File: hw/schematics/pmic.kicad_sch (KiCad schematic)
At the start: 40 parts, among them J1 TYPE-C-31-M-13C, J2 Conn_01x02, U2 NPM1300-QEAA-R

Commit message: apply 0603 footprint
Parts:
- C1, C10, C2, C3, C4, C5, C6, C7, C8, C9, R1, R13, R14, R2, R4, rC1, rC10, rC2, rC3, rC4, rC5, rC6, rC7, rC8, rC9, rR1, rR13, rR14, rR2, rR4: footprint (none) -> Alidade:SMD_0603
- L1, L2, rL1, rL2: value 2.2u -> 2.2uH; footprint (none) -> Alidade:SMD_0603
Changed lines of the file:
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@@
 			)
 		)
-		(property "Value" "2.2u"
+		(property "Value" "2.2uH"
 			(at 44.4181 145.034 90)
 			(effects
@@
 			)
 		)
-		(property "Footprint" ""
+		(property "Footprint" "Alidade:SMD_0603"
 			(at 44.45 143.51 0)
 			(effects
@@
 			)
 		)
-		(property "Footprint" ""
+		(property "Footprint" "Alidade:SMD_0603"
 			(at 367.03 148.59 0)
 			(effects
@@
 			)
 		)
-		(property "Footprint" ""
+		(property "Footprint" "Alidade:SMD_0603"
 			(at 265.43 148.59 0)
 			(effects
@@
 			)
 		)
-		(property "Footprint" ""
+		(property "Footprint" "Alidade:SMD_0603"
 			(at 374.65 148.59 0)
 			(effects
@@
 			)
 		)
-		(property "Footprint" ""
+		(property "Footprint" "Alidade:SMD_0603"
 			(at 212.09 236.22 0)
 			(effects
@@
 			)
 		)
-		(property "Value" "2.2u"
+		(property "Value" "2.2uH"
 			(at 139.446 148.59 90)
 			(effects
@@
 			)
 		)
-		(property "Footprint" ""
+		(property "Footprint" "Alidade:SMD_0603"
 			(at 139.7 147.32 0)
 			(effects
@@
 			)
 		)
-		(property "Footprint" ""
+		(property "Footprint" "Alidade:SMD_0603"
 			(at 273.05 148.59 0)
 			(effects
@@
 			)
 		)
-		(property "Footprint" ""
+		(property "Footprint" "Alidade:SMD_0603"
 			(at 355.6 49.53 0)
 			(effects
@@
 			)
 		)
-		(property "Footprint" ""
+		(property "Footprint" "Alidade:SMD_0603"
 			(at 257.81 148.59 0)
 			(effects
@@
 			)
 		)
-		(property "Footprint" ""
+		(property "Footprint" "Alidade:SMD_0603"
 			(at 351.79 148.59 0)
 			(effects
@@
 			)
 		)
-		(property "Footprint" ""
+		(property "Footprint" "Alidade:SMD_0603"
 			(at 250.19 148.59 0)
 			(effects
@@
 			)
 		)
-		(property "Footprint" ""
+		(property "Footprint" "Alidade:SMD_0603"
 			(at 359.41 148.59 0)
 			(effects
@@
 			)
 		)
-		(property "Footprint" ""
+		(property "Footprint" "Alidade:SMD_0603"
 			(at 284.48 48.26 0)
 			(effects
@@
 			)
 		)
-		(property "Footprint" ""
+		(property "Footprint" "Alidade:SMD_0603"
 			(at 205.74 236.22 0)
 			(effects
@@
 			)
 		)
-		(property "Footprint" ""
+		(property "Footprint" "Alidade:SMD_0603"
 			(at 142.24 153.67 0)
 			(effects
@@
 			)
 		)
-		(property "Footprint" ""
+		(property "Footprint" "Alidade:SMD_0603"
 			(at 295.91 148.59 0)
 			(effects
@@
 			)
 		)
-		(property "Footprint" ""
+		(property "Footprint" "Alidade:SMD_0603"
 			(at 321.31 148.59 0)
 			(effects
@@
 			)
 		)
-		(property "Footprint" ""
+		(property "Footprint" "Alidade:SMD_0603"
 			(at 46.99 149.86 0)
 			(effects
@@
 			)
 		)
-		(property "Footprint" ""
+		(property "Footprint" "Alidade:SMD_0603"
 			(at 288.29 148.59 0)
 			(effects
@@
 			)
 		)
-		(property "Footprint" ""
+		(property "Footprint" "Alidade:SMD_0603"
 			(at 87.63 148.59 0)
 			(effects
@@
 			)
 		)
-		(property "Footprint" ""
+		(property "Footprint" "Alidade:SMD_0603"
 			(at 328.93 148.59 0)
 			(effects
@@
 			)
 		)
-		(property "Footprint" ""
+		(property "Footprint" "Alidade:SMD_0603"
 			(at 234.95 148.59 0)
 			(effects
@@
 			)
 		)
-		(property "Footprint" ""
+		(property "Footprint" "Alidade:SMD_0603"
 			(at 279.4 237.49 0)
 			(effects
@@
 			)
 		)
-		(property "Value" "2.2u"
+		(property "Value" "2.2uH"
 			(at 84.582 144.018 90)
 			(effects
@@
 			)
 		)
-		(property "Footprint" ""
+		(property "Footprint" "Alidade:SMD_0603"
 			(at 85.09 142.24 0)
 			(effects
@@
 			)
 		)
-		(property "Footprint" ""
+		(property "Footprint" "Alidade:SMD_0603"
 			(at 382.27 148.59 0)
 			(effects
@@
 			)
 		)
-		(property "Footprint" ""
+		(property "Footprint" "Alidade:SMD_0603"
 			(at 280.67 148.59 0)
 			(effects
@@
 			)
 		)
-		(property "Footprint" ""
+		(property "Footprint" "Alidade:SMD_0603"
 			(at 303.53 148.59 0)
 			(effects
@@
 			)
 		)
-		(property "Value" "2.2u"
+		(property "Value" "2.2uH"
 			(at 182.372 147.32 90)
 			(effects
@@
 			)
 		)
-		(property "Footprint" ""
+		(property "Footprint" "Alidade:SMD_0603"
 			(at 182.88 146.05 0)
 			(effects
@@
 			)
 		)
-		(property "Footprint" ""
+		(property "Footprint" "Alidade:SMD_0603"
 			(at 389.89 148.59 0)
 			(effects
@@
 			)
 		)
-		(property "Footprint" ""
+		(property "Footprint" "Alidade:SMD_0603"
 			(at 285.75 237.49 0)
 			(effects
@@
 			)
 		)
-		(property "Footprint" ""
+		(property "Footprint" "Alidade:SMD_0603"
 			(at 185.42 152.4 0)
 			(effects
@@
 			)
 		)
-		(property "Footprint" ""
+		(property "Footprint" "Alidade:SMD_0603"
 			(at 336.55 148.59 0)
 			(effects
@@
 			)
 		)
-		(property "Footprint" ""
+		(property "Footprint" "Alidade:SMD_0603"
 			(at 344.17 148.59 0)
 			(effects
@@
 			)
 		)
-		(property "Footprint" ""
+		(property "Footprint" "Alidade:SMD_0603"
 			(at 242.57 148.59 0)
 			(effects

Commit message: add some LCSC part numbers
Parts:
- J1, rJ1: JLCPCB Part # C2848620 -> (none); LCSC Part # (none) -> C2848620

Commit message: Use bat54 instead
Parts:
- U2, rU2: LCSC Part # (none) -> C7466043
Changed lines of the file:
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@@
 			)
 		)
-		(property "JLCPCB Part #" ""
+		(property "LCSC Part #" "C7466043"
 			(at 266.7 91.44 0)
 			(effects
@@
 			)
 		)
-		(property "JLCPCB Part #" ""
+		(property "LCSC Part #" "C7466043"
 			(at 289.56 43.18 0)
 			(effects
@@
 			)
 		)
-		(property "Datasheet" "~"
+		(property "Datasheet" ""
 			(at 271.78 45.72 0)
 			(effects
@@
 			)
 		)
+		(property "LCSC Part #" "C7466043"
+			(at 360.68 44.45 0)
+			(effects
+				(font
+					(size 1.27 1.27)
+				)
+				(hide yes)
+			)
+		)
 		(pin "31"
 		)
@@
 			)
 		)
-		(property "JLCPCB Part #" ""
+		(property "LCSC Part #" "C7466043"
 			(at 86.36 46.99 0)
 			(effects
@@
 			)
 		)
-		(property "JLCPCB Part #" ""
+		(property "LCSC Part #" "C7466043"
 			(at 77.47 224.79 0)
 			(effects
@@
 			)
 		)
+		(property "LCSC Part #" "C7466043"
+			(at 191.77 45.72 0)
+			(effects
+				(font
+					(size 1.27 1.27)
+				)
+				(hide yes)
+			)
+		)
 		(pin "31"
 		)
@@
 			)
 		)
-		(property "JLCPCB Part #" ""
+		(property "LCSC Part #" "C7466043"
 			(at 48.26 138.43 0)
 			(effects
@@
 			)
 		)
-		(property "Datasheet" "~"
+		(property "Datasheet" ""
 			(at 342.9 46.99 0)
 			(effects
@@
 			)
 		)
+		(property "LCSC Part #" "C7466043"
+			(at 293.37 237.49 0)
+			(effects
+				(font
+					(size 1.27 1.27)
+				)
+				(hide yes)
+			)
+		)
 		(pin "31"
 		)
@@
 			)
 		)
-		(property "JLCPCB Part #" ""
+		(property "LCSC Part #" "C7466043"
 			(at 287.02 189.23 0)
 			(effects
@@
 			)
 		)
+		(property "LCSC Part #" "C7466043"
+			(at 354.33 87.63 0)
+			(effects
+				(font
+					(size 1.27 1.27)
+				)
+				(hide yes)
+			)
+		)
 		(pin "31"
 		)
@@
 			)
 		)
+		(property "LCSC Part #" "C7466043"
+			(at 186.69 140.97 0)
+			(effects
+				(font
+					(size 1.27 1.27)
+				)
+				(hide yes)
+			)
+		)
 		(pin "31"
 		)
@@
 			)
 		)
+		(property "LCSC Part #" "C7466043"
+			(at 345.44 190.5 0)
+			(effects
+				(font
+					(size 1.27 1.27)
+				)
+				(hide yes)
+			)
+		)
 		(pin "31"
 		)
@@
 			)
 		)
-		(property "JLCPCB Part #" ""
+		(property "LCSC Part #" "C7466043"
 			(at 143.51 142.24 0)
 			(effects
@@
 			)
 		)
+		(property "LCSC Part #" "C7466043"
+			(at 88.9 137.16 0)
+			(effects
+				(font
+					(size 1.27 1.27)
+				)
+				(hide yes)
+			)
+		)
 		(pin "31"
 		)
@@
 			)
 		)
-		(property "JLCPCB Part #" ""
+		(property "LCSC Part #" "C7466043"
 			(at 219.71 236.22 0)
 			(effects
@@
 			(at 138.43 226.06 0)
 			(effects
+				(font
+					(size 1.27 1.27)
+				)
+				(hide yes)
+			)
+		)
+		(property "LCSC Part #" "C7466043"
+			(at 138.43 226.06 0)
+			(effects

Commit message: add some LCSC part numbers
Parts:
- C1, C10, rC1, rC10: footprint Alidade:SMD_0603 -> Alidade:0603; LCSC Part # (none) -> C15849
- C2, rC2: footprint Alidade:SMD_0603 -> Alidade:0603; LCSC Part # (none) -> C23630
- C3, C4, C5, C6, C7, C8, C9, rC3, rC4, rC5, rC6, rC7, rC8, rC9: footprint Alidade:SMD_0603 -> Alidade:0603; LCSC Part # (none) -> C96446
- L1, L2, rL1, rL2: footprint Alidade:SMD_0603 -> Alidade:0603
- R1, rR1: footprint Alidade:SMD_0603 -> Alidade:0603; LCSC Part # (none) -> C25819
- R13, R14, R4, rR13, rR14, rR4: footprint Alidade:SMD_0603 -> Alidade:0603; LCSC Part # (none) -> C25804
- R2, rR2: footprint Alidade:SMD_0603 -> Alidade:0603; LCSC Part # (none) -> C21189

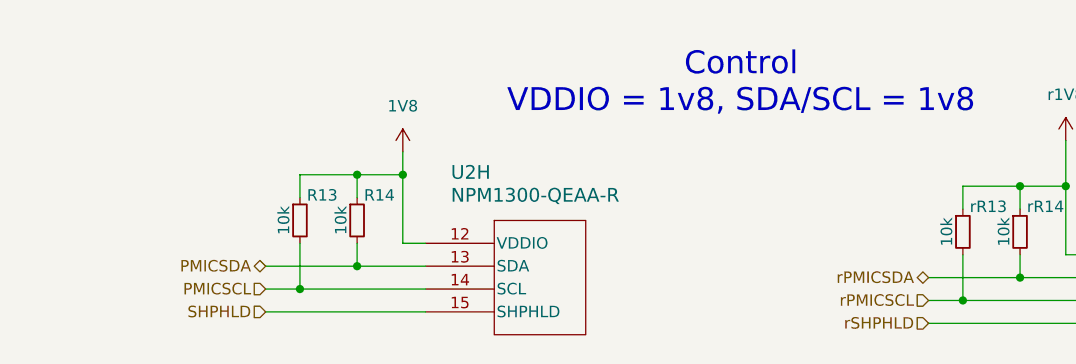
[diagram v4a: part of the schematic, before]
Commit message: Update symbol, use ads122S for bridge measurement
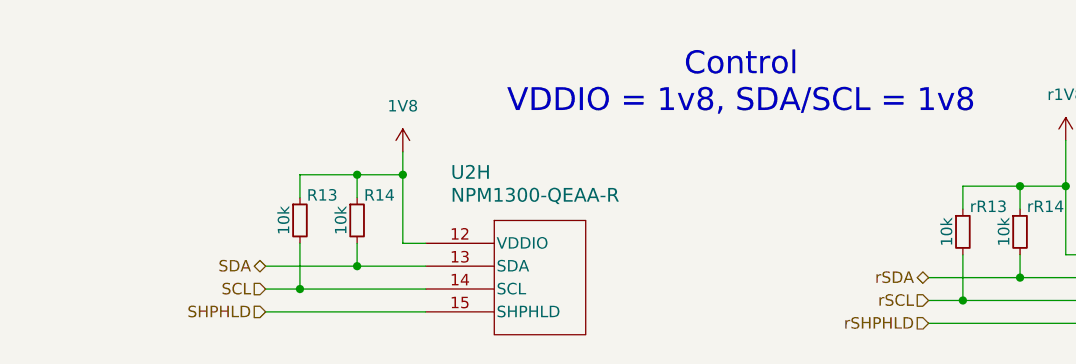
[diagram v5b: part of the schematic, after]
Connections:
- net PMICSCL renamed SCL
- net PMICSDA renamed SDA
- net rPMICSCL renamed rSCL
- net rPMICSDA renamed rSDA
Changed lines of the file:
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@@
 		)
 	)
-	(hierarchical_label "rPMICSCL"
+	(hierarchical_label "rSCL"
 		(shape input)
 		(at 275.59 245.11 180)
@@
 		)
 	)
-	(hierarchical_label "PMICSDA"
+	(hierarchical_label "SDA"
 		(shape bidirectional)
 		(at 201.93 241.3 180)
@@
 		)
 	)
-	(hierarchical_label "rPMICSDA"
+	(hierarchical_label "rSDA"
 		(shape bidirectional)
 		(at 275.59 242.57 180)
@@
 		)
 	)
-	(hierarchical_label "PMICSCL"
+	(hierarchical_label "SCL"
 		(shape input)
 		(at 201.93 243.84 180)

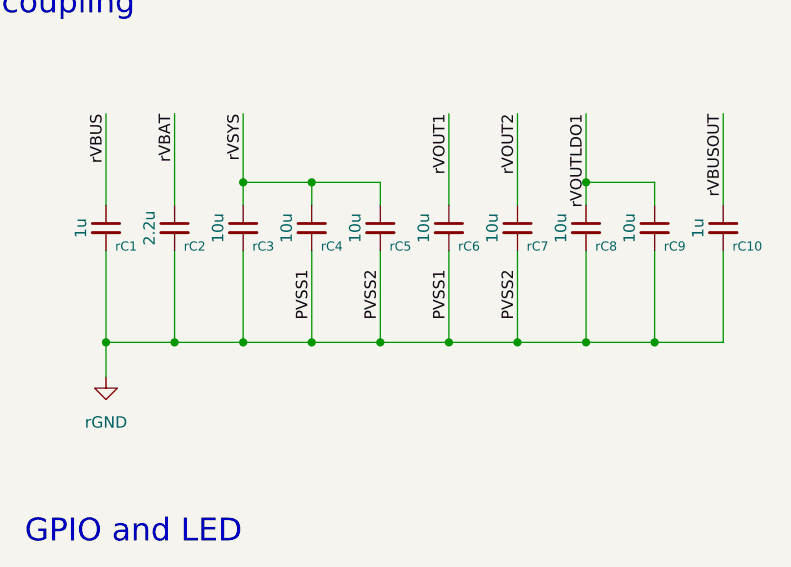
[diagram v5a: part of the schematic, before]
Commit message: Solve erc errors
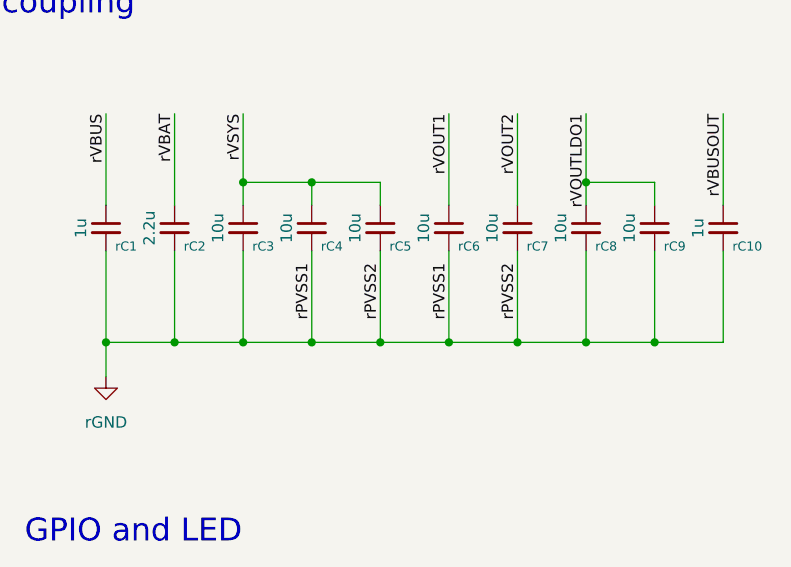
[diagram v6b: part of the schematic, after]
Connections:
- net GND: no longer rC1.2, rC10.2, rC2.2, rC3.2, rC4.2, rC5.2, rC6.2, rC7.2, rC8.2, rC9.2, rJ1.A1 (GND), rJ1.A12 (GND), rJ1.B1 (GND), rJ1.B12 (GND), rJ1.S1 (SHIELD), rJ2.2 (Pin_2), rR1.1, rR2.1, rR4.1, rU2.2 (PVSS1), rU2.33 (AVSS), rU2.6 (PVSS2)
- new net rGND: rC1.2, rC10.2, rC2.2, rC3.2, rC4.2, rC5.2, rC6.2, rC7.2, rC8.2, rC9.2, rJ1.A1 (GND), rJ1.A12 (GND), rJ1.B1 (GND), rJ1.B12 (GND), rJ1.S1 (SHIELD), rJ2.2 (Pin_2), rR1.1, rR2.1, rR4.1, rU2.2 (PVSS1), rU2.33 (AVSS), rU2.6 (PVSS2)
